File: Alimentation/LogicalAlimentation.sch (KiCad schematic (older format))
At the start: 13 parts

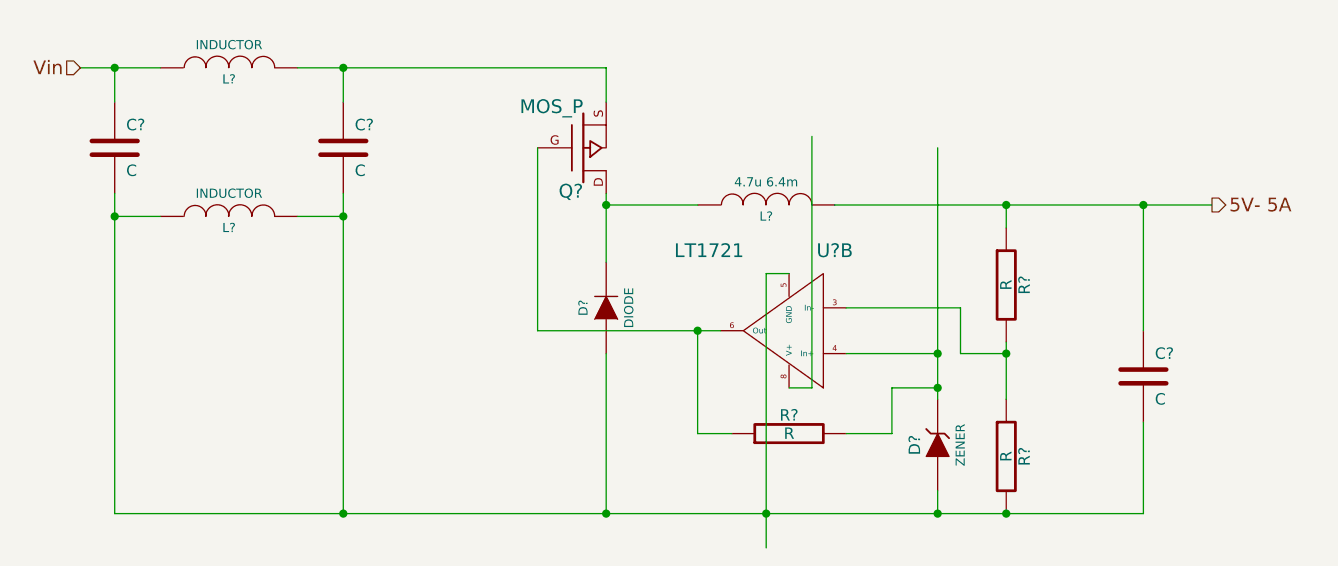
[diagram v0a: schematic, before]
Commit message: Adding board for alimentation
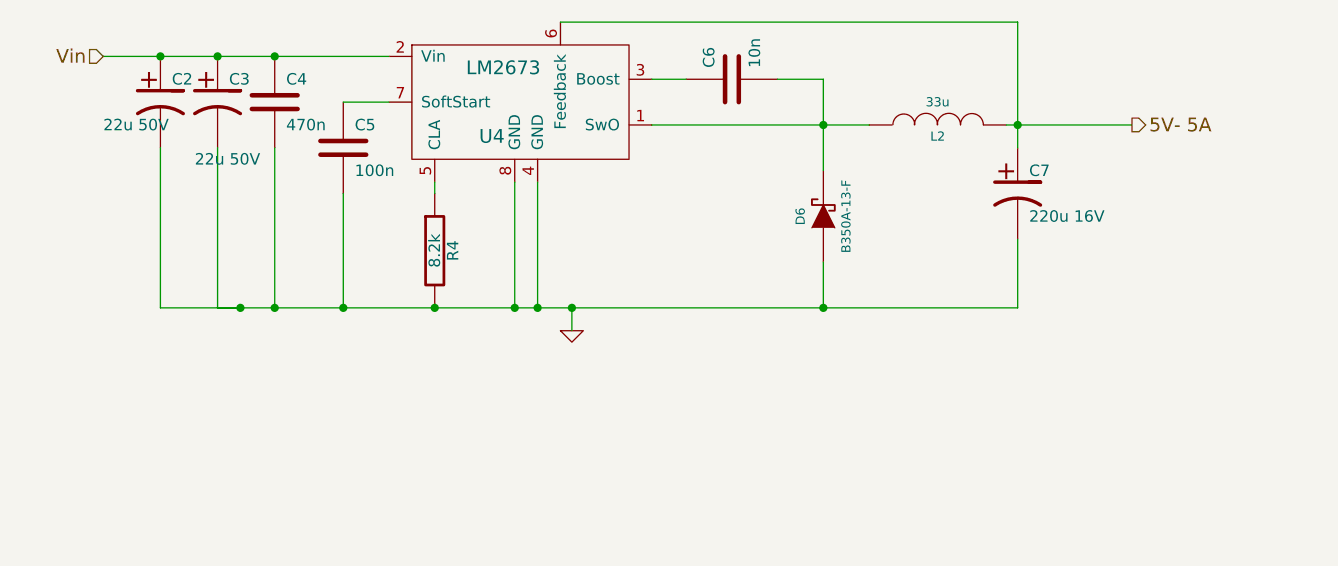
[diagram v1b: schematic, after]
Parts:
- removed C? (x3): C, symbol C
- removed D?: DIODE, symbol DIODE
- removed D?: ZENER, symbol ZENER
- removed L? (x2): INDUCTOR, symbol INDUCTOR
- removed L?: 4.7u 6.4m, symbol INDUCTOR
- removed Q?: MOS_P, symbol MOS_P
- removed R? (x3): R, symbol R
- removed U?: LT1721, symbol LT1721
- added C2, C3: 22u 50V, symbol CP1
- added C4: 470n, symbol C
- added C5: 100n, symbol C
- added C6: 10n, symbol C
- added C7: 220u 16V, symbol CP1
- added D6: B350A-13-F, symbol DIODESCH
- added L2: 33u, symbol INDUCTOR
- added R4: 8.2k, symbol R
- added U4: LM2673, symbol LM2673
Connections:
- net labels added: GND
- wire segments 35 -> 21

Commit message: Add 5V LDO for logic part of motor alimentation
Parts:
- added R17: 1k, symbol R
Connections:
- net 5V- 5A: now also R17.2
- net GND: now also R17.1
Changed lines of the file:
@@
 U 1 1 5326CC54
 P 5550 3500
-F 0 "U4" H 5450 3350 60  0000 C CNN
+F 0 "U4" H 6000 3200 60  0000 C CNN
 F 1 "LM2673" H 5500 3650 60  0000 C CNN
 F 2 "" H 5550 3500 60  0001 C CNN
@@
 	5550 3850 5550 4400
 Connection ~ 5550 4400
+$Comp
+L R R17
+U 1 1 53A991FC
+P 7300 4050
+F 0 "R17" V 7380 4050 50  0000 C CNN
+F 1 "1k" V 7300 4050 50  0000 C CNN
+F 2 "" H 7300 4050 60  0001 C CNN
+F 3 "" H 7300 4050 60  0001 C CNN
+	1    7300 4050
+	1    0    0    1
+$EndComp
+Wire Wire Line
+	7300 3800 7300 3150
+Connection ~ 7300 3150
+Wire Wire Line
+	7300 4300 7300 4400
+Connection ~ 7300 4400
 $EndSCHEMATC
